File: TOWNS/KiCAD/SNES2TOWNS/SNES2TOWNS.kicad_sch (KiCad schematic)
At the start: 7 parts, among them J1 DE9_Receptacle, J2 Conn_01x06_Pin, J3 Conn_01x06_Pin, J4 Conn_01x06_Pin, J5 Conn_01x06_Pin, U1 74LS157, U2 74LS157

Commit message: Added bypass capacitor.
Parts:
- added C1, C2: 0.1uF, symbol Device:C
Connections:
- net +5V: now also C1.1, C2.1
- net GND: now also C1.2, C2.2
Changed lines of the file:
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@@
   (junction (at 153.67 91.44) (diameter 0) (color 0 0 0 0)
   )
+  (junction (at 242.57 95.25) (diameter 0) (color 0 0 0 0)
+  )
   (junction (at 226.06 95.25) (diameter 0) (color 0 0 0 0)
   )
@@
   )
   (junction (at 162.56 124.46) (diameter 0) (color 0 0 0 0)
+  )
+  (junction (at 223.52 81.28) (diameter 0) (color 0 0 0 0)
+  )
+  (junction (at 229.87 95.25) (diameter 0) (color 0 0 0 0)
+  )
+  (junction (at 229.87 109.22) (diameter 0) (color 0 0 0 0)
   )
   (junction (at 63.5 59.69) (diameter 0) (color 0 0 0 0)
@@
     (stroke (width 0) (type default))
   )
+  (wire (pts (xy 229.87 95.25) (xy 242.57 95.25))
+    (stroke (width 0) (type default))
+  )
   (wire (pts (xy 201.93 69.85) (xy 218.44 69.85))
     (stroke (width 0) (type default))
@@
     (stroke (width 0) (type default))
   )
+  (wire (pts (xy 242.57 95.25) (xy 242.57 101.6))
+    (stroke (width 0) (type default))
+  )
   (wire (pts (xy 162.56 87.63) (xy 162.56 121.92))
     (stroke (width 0) (type default))
@@
     (stroke (width 0) (type default))
   )
+  (wire (pts (xy 223.52 109.22) (xy 229.87 109.22))
+    (stroke (width 0) (type default))
+  )
   (wire (pts (xy 142.24 109.22) (xy 176.53 109.22))
     (stroke (width 0) (type default))
@@
     (stroke (width 0) (type default))
   )
-  (wire (pts (xy 226.06 95.25) (xy 271.78 95.25))
+  (wire (pts (xy 226.06 95.25) (xy 229.87 95.25))
     (stroke (width 0) (type default))
   )
@@
     (stroke (width 0) (type default))
   )
+  (wire (pts (xy 229.87 109.22) (xy 242.57 109.22))
+    (stroke (width 0) (type default))
+  )
   (wire (pts (xy 201.93 62.23) (xy 220.98 62.23))
     (stroke (width 0) (type default))
@@
     (stroke (width 0) (type default))
   )
+  (wire (pts (xy 223.52 81.28) (xy 241.3 81.28))
+    (stroke (width 0) (type default))
+  )
   (wire (pts (xy 212.09 106.68) (xy 212.09 73.66))
     (stroke (width 0) (type default))
   )
-  (wire (pts (xy 204.47 81.28) (xy 241.3 81.28))
+  (wire (pts (xy 204.47 81.28) (xy 223.52 81.28))
     (stroke (width 0) (type default))
   )
@@
   )
   (wire (pts (xy 204.47 81.28) (xy 204.47 87.63))
+    (stroke (width 0) (type default))
+  )
+  (wire (pts (xy 229.87 95.25) (xy 229.87 101.6))
+    (stroke (width 0) (type default))
+  )
+  (wire (pts (xy 223.52 81.28) (xy 223.52 109.22))
+    (stroke (width 0) (type default))
+  )
+  (wire (pts (xy 242.57 95.25) (xy 271.78 95.25))
     (stroke (width 0) (type default))
   )
@@
     )
   )
+  (symbol (lib_id "Device:C") (at 229.87 105.41 0) (unit 1)
+    (in_bom yes) (on_board yes) (dnp no) (fields_autoplaced)
+    (property "Reference" "C1" (at 233.68 104.14 0)
+      (effects (font (size 1.27 1.27)) (justify left))
+    )
+    (property "Value" "0.1uF" (at 233.68 106.68 0)
+      (effects (font (size 1.27 1.27)) (justify left))
+    )
+    (property "Footprint" "" (at 230.8352 109.22 0)
+      (effects (font (size 1.27 1.27)) hide)
+    )
+    (property "Datasheet" "~" (at 229.87 105.41 0)
+      (effects (font (size 1.27 1.27)) hide)
+    )
+    (pin "1")
+    (pin "2")
+    (instances
+      (project "SNES2TOWNS"
+        (path "/d12ccb08-8752-4d3d-ad3b-4f570691df19"
+          (reference "C1") (unit 1)
+        )
+      )
+    )
+  )
   (symbol (lib_id "Connector:DE9_Receptacle") (at 248.92 73.66 0) (unit 1)
     (in_bom yes) (on_board yes) (dnp no) (fields_autoplaced)
@@
         )
       )
+    )
+  )
+  (symbol (lib_id "Device:C") (at 242.57 105.41 0) (unit 1)
+    (in_bom yes) (on_board yes) (dnp no) (fields_autoplaced)
+    (property "Reference" "C2" (at 246.38 104.14 0)
+      (effects (font (size 1.27 1.27)) (justify left))
+    )
+    (property "Value" "0.1uF" (at 246.38 106.68 0)
+      (effects (font (size 1.27 1.27)) (justify left))
+    )
+    (property "Footprint" "" (at 243.5352 109.22 0)
+      (effects (font (size 1.27 1.27)) hide)
+    )
+    (property "Datasheet" "~" (at 242.57 105.41 0)
+      (effects (font (size 1.27 1.27)) hide)
+    )
+    (pin "1")
+    (pin "2")
+    (instances
+      (project "SNES2TOWNS"
+        (path "/d12ccb08-8752-4d3d-ad3b-4f570691df19"
+          (reference "C2") (unit 1)
+        )
+      )

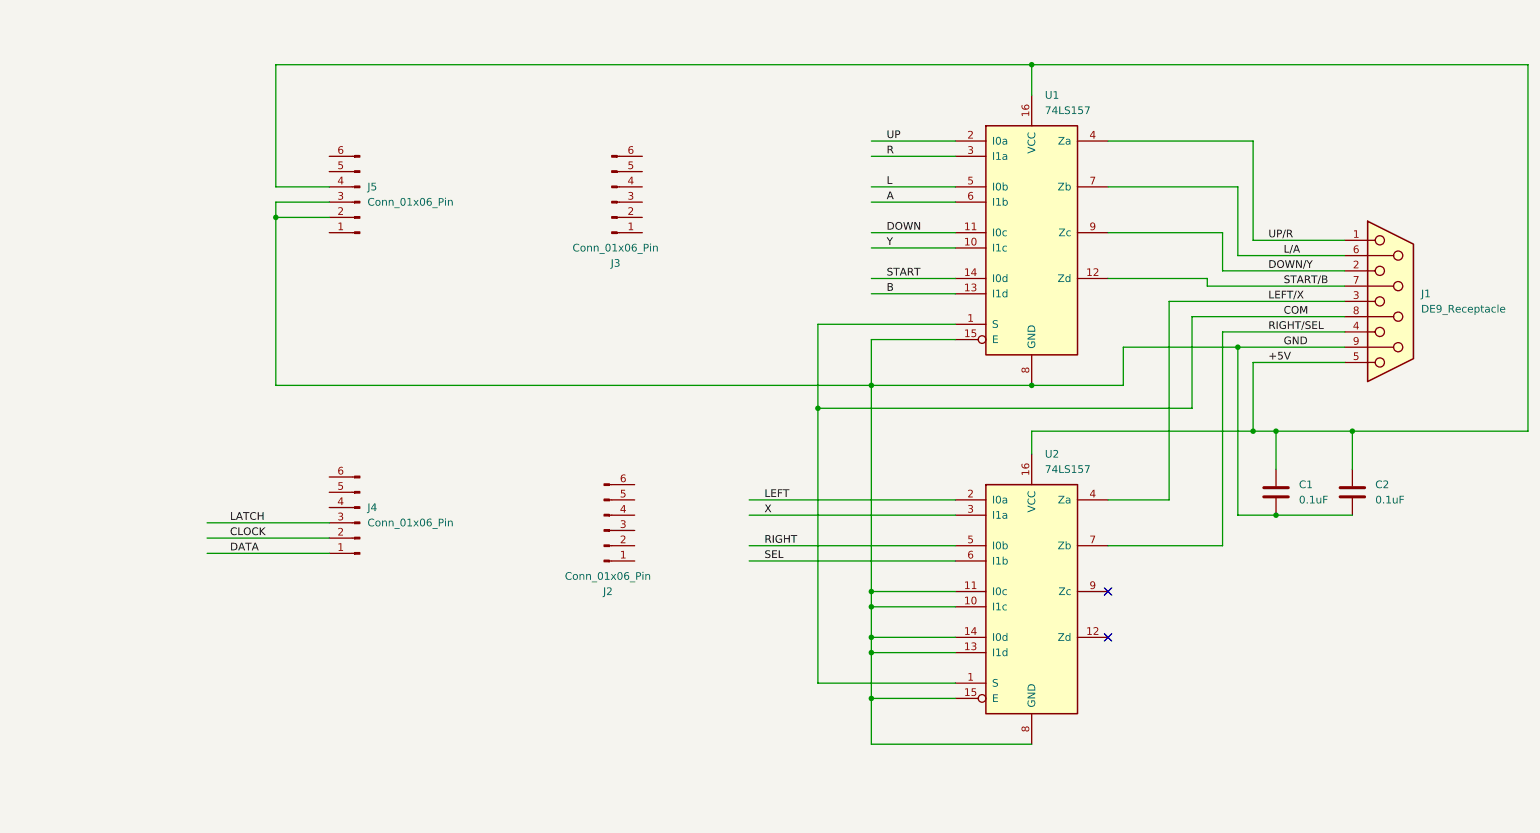
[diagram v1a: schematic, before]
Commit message: SNES to TOWNS Controller Adapter
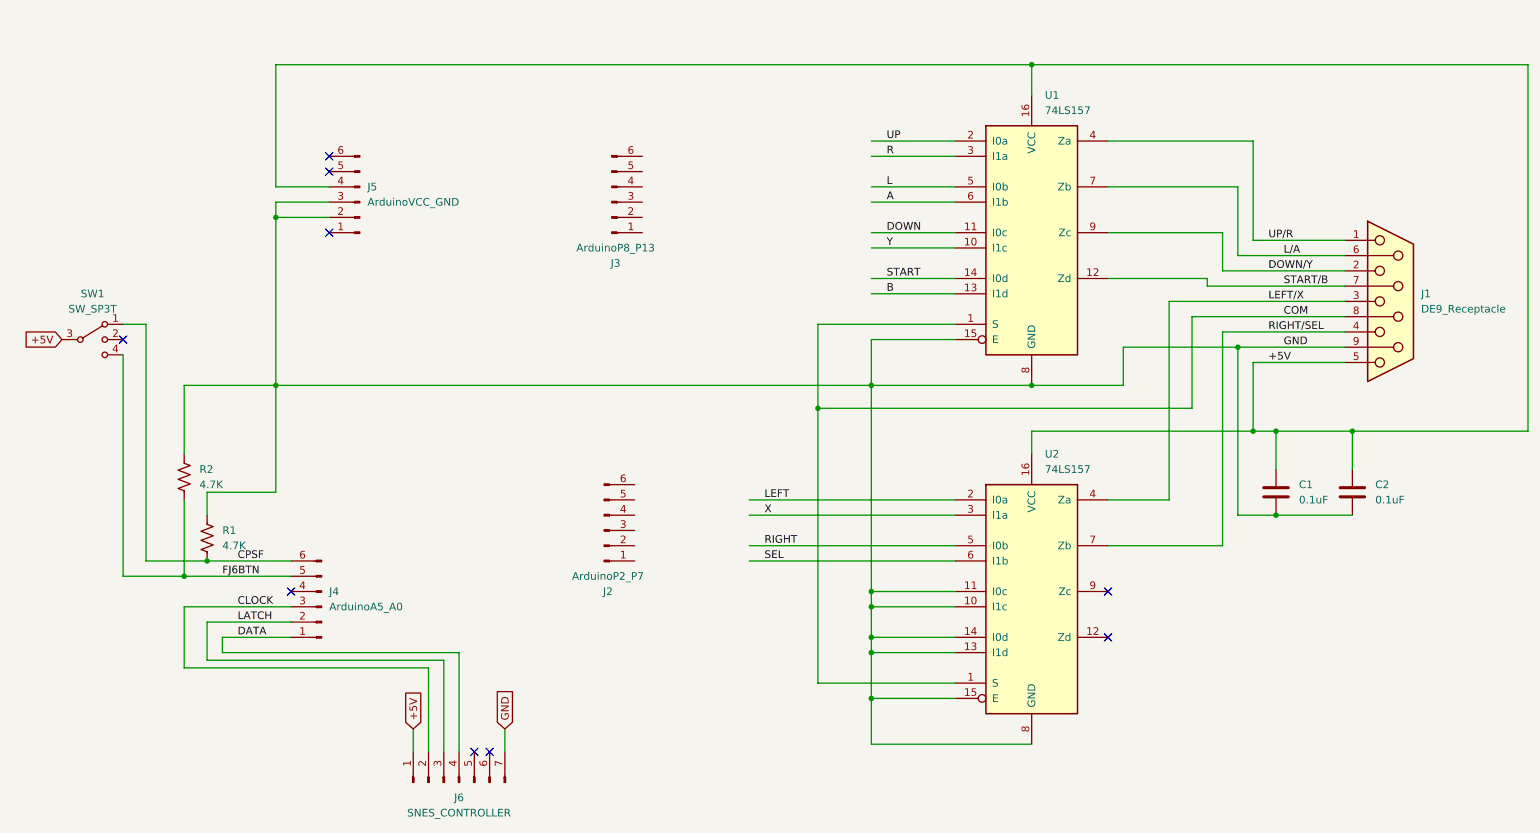
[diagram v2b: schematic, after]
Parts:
- added J6: SNES_CONTROLLER, symbol Connector:Conn_01x07_Pin
- added R1, R2: 4.7K, symbol Device:R_US
- added SW1: SW_SP3T, symbol Switch:SW_SP3T
- J2: value Conn_01x06_Pin -> ArduinoP2_P7
- J3: value Conn_01x06_Pin -> ArduinoP8_P13
- J4: value Conn_01x06_Pin -> ArduinoA5_A0
- J5: value Conn_01x06_Pin -> ArduinoVCC_GND
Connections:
- net +5V: now also J6.1 (Pin_1), SW1.3
- net CLOCK: now also J4.3 (Pin_3), J6.2 (Pin_2); no longer J4.2 (Pin_2)
- net DATA: now also J6.4 (Pin_4)
- net GND: now also J6.7 (Pin_7), R1.1, R2.1
- net LATCH: now also J4.2 (Pin_2), J6.3 (Pin_3); no longer J4.3 (Pin_3)
- net FJ6BTN: now reaches J4.5 (Pin_5)
- net FJ6BTN: now also R2.2, SW1.4
- net CPSF: now reaches J4.6 (Pin_6)
- net CPSF: now also R1.2, SW1.1
- no-connect marks 2 -> 9
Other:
- moved on the sheet: J4

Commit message: Rough PCB placements
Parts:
- removed SW1: SW_SP3T, symbol Switch:SW_SP3T
- added J7: Conn_02x03_Odd_Even, Connector_PinHeader_2.54mm:PinHeader_2x03_P2.54mm_Vertical, symbol Connector_Generic:Conn_02x03_Odd_Even
- C1, C2: footprint (none) -> Capacitor_THT:C_Disc_D5.0mm_W2.5mm_P5.00mm
- J1: footprint (none) -> Connector_Dsub:DSUB-9_Female_Vertical_P2.77x2.84mm
- J2, J3, J4, J5: footprint (none) -> Connector_PinHeader_2.54mm:PinHeader_1x06_P2.54mm_Vertical
- J6: footprint (none) -> Connector_PinHeader_2.54mm:PinHeader_1x07_P2.54mm_Vertical
- R1, R2: footprint (none) -> Resistor_THT:R_Axial_DIN0207_L6.3mm_D2.5mm_P10.16mm_Horizontal
- U1, U2: footprint (none) -> Package_DIP:DIP-16_W7.62mm_Socket
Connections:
- net +5V: now also J7.3 (Pin_3), J7.4 (Pin_4)
- net CPSF: now also J7.1 (Pin_1), J7.2 (Pin_2)
- net FJ6BTN: now also J7.5 (Pin_5), J7.6 (Pin_6)
- no-connect marks 9 -> 8
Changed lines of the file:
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@@
   (junction (at 162.56 121.92) (diameter 0) (color 0 0 0 0)
   )
+  (junction (at 38.1 87.63) (diameter 0) (color 0 0 0 0)
+  )
   (junction (at 162.56 132.08) (diameter 0) (color 0 0 0 0)
   )
+  (junction (at 44.45 80.01) (diameter 0) (color 0 0 0 0)
+  )
   (junction (at 52.07 116.84) (diameter 0) (color 0 0 0 0)
   )
@@
   )
   (junction (at 48.26 119.38) (diameter 0) (color 0 0 0 0)
+  )
+  (junction (at 38.1 77.47) (diameter 0) (color 0 0 0 0)
   )
   (junction (at 63.5 87.63) (diameter 0) (color 0 0 0 0)
@@
   (no_connect (at 66.04 121.92))
   (no_connect (at 99.06 148.59))
-  (no_connect (at 38.1 80.01))
   (no_connect (at 96.52 148.59))
   (no_connect (at 72.39 52.07))
@@
     (stroke (width 0) (type default))
   )
+  (wire (pts (xy 38.1 71.12) (xy 25.4 71.12))
+    (stroke (width 0) (type default))
+  )
   (wire (pts (xy 271.78 95.25) (xy 271.78 34.29))
     (stroke (width 0) (type default))
@@
     (stroke (width 0) (type default))
   )
+  (wire (pts (xy 44.45 80.01) (xy 45.72 80.01))
+    (stroke (width 0) (type default))
+  )
   (wire (pts (xy 201.93 54.61) (xy 223.52 54.61))
     (stroke (width 0) (type default))
   )
+  (wire (pts (xy 38.1 77.47) (xy 38.1 71.12))
+    (stroke (width 0) (type default))
+  )
   (wire (pts (xy 162.56 46.99) (xy 176.53 46.99))
     (stroke (width 0) (type default))
@@
     (stroke (width 0) (type default))
   )
+  (wire (pts (xy 25.4 71.12) (xy 25.4 77.47))
+    (stroke (width 0) (type default))
+  )
   (wire (pts (xy 218.44 69.85) (xy 218.44 71.12))
     (stroke (width 0) (type default))
@@
     (stroke (width 0) (type default))
   )
+  (wire (pts (xy 44.45 67.31) (xy 21.59 67.31))
+    (stroke (width 0) (type default))
+  )
   (wire (pts (xy 220.98 114.3) (xy 220.98 78.74))
     (stroke (width 0) (type default))
@@
     (stroke (width 0) (type default))
   )
+  (wire (pts (xy 21.59 80.01) (xy 25.4 80.01))
+    (stroke (width 0) (type default))
+  )
   (wire (pts (xy 226.06 46.99) (xy 226.06 63.5))
     (stroke (width 0) (type default))
@@
     (stroke (width 0) (type default))
   )
+  (wire (pts (xy 21.59 67.31) (xy 21.59 80.01))
+    (stroke (width 0) (type default))
+  )
   (wire (pts (xy 189.23 34.29) (xy 189.23 39.37))
     (stroke (width 0) (type default))
@@
     (stroke (width 0) (type default))
   )
+  (wire (pts (xy 25.4 82.55) (xy 25.4 87.63))
+    (stroke (width 0) (type default))
+  )
   (wire (pts (xy 38.1 77.47) (xy 41.91 77.47))
     (stroke (width 0) (type default))
@@
     (stroke (width 0) (type default))
   )
+  (wire (pts (xy 38.1 87.63) (xy 38.1 119.38))
+    (stroke (width 0) (type default))
+  )
   (wire (pts (xy 223.52 81.28) (xy 241.3 81.28))
     (stroke (width 0) (type default))
@@
     (stroke (width 0) (type default))
   )
+  (wire (pts (xy 38.1 80.01) (xy 44.45 80.01))
+    (stroke (width 0) (type default))
+  )
   (wire (pts (xy 54.61 132.08) (xy 93.98 132.08))
     (stroke (width 0) (type default))
@@
     (stroke (width 0) (type default))
   )
-  (wire (pts (xy 38.1 82.55) (xy 38.1 119.38))
+  (wire (pts (xy 38.1 82.55) (xy 38.1 87.63))
     (stroke (width 0) (type default))
   )
@@
     (stroke (width 0) (type default))
   )
+  (wire (pts (xy 25.4 87.63) (xy 38.1 87.63))
+    (stroke (width 0) (type default))
+  )
   (wire (pts (xy 204.47 81.28) (xy 204.47 87.63))
     (stroke (width 0) (type default))
@@
     (stroke (width 0) (type default))
   )
+  (wire (pts (xy 44.45 80.01) (xy 44.45 67.31))
+    (stroke (width 0) (type default))
+  )
   (wire (pts (xy 223.52 66.04) (xy 241.3 66.04))
     (stroke (width 0) (type default))
@@
     (effects (font (size 1.27 1.27)) (justify left bottom))
   )
-  (global_label "+5V" (shape input) (at 27.94 80.01 180) (fields_autoplaced)
-    (effects (font (size 1.27 1.27)) (justify right))
-    (property "Intersheetrefs" "${INTERSHEET_REFS}" (at 21.0843 80.01 0)
-      (effects (font (size 1.27 1.27)) (justify right) hide)
+  (global_label "+5V" (shape input) (at 45.72 80.01 0) (fields_autoplaced)
+    (effects (font (size 1.27 1.27)) (justify left))
+    (property "Intersheetrefs" "${INTERSHEET_REFS}" (at 52.5757 80.01 0)
+      (effects (font (size 1.27 1.27)) (justify left) hide)
     )
   )
@@
       (effects (font (size 1.27 1.27)))
     )
-    (property "Footprint" "" (at 93.98 153.67 0)
+    (property "Footprint" "Connector_PinHeader_2.54mm:PinHeader_1x07_P2.54mm_Vertical" (at 93.98 153.67 0)
       (effects (font (size 1.27 1.27)) hide)
     )
@@
       (effects (font (size 1.27 1.27)) (justify left))
     )
-    (property "Footprint" "" (at 189.23 121.92 0)
+    (property "Footprint" "Package_DIP:DIP-16_W7.62mm_Socket" (at 189.23 121.92 0)
       (effects (font (size 1.27 1.27)) hide)
     )
@@
       (effects (font (size 1.27 1.27)))
     )
-    (property "Footprint" "" (at 118.11 111.76 0)
+    (property "Footprint" "Connector_PinHeader_2.54mm:PinHeader_1x06_P2.54mm_Vertical" (at 118.11 111.76 0)
       (effects (font (size 1.27 1.27)) hide)
     )
@@
       (effects (font (size 1.27 1.27)) (justify left))
     )
-    (property "Footprint" "" (at 49.276 103.124 90)
+    (property "Footprint" "Resistor_THT:R_Axial_DIN0207_L6.3mm_D2.5mm_P10.16mm_Horizontal" (at 49.276 103.124 90)
       (effects (font (size 1.27 1.27)) hide)
     )
@@
       (effects (font (size 1.27 1.27)) (justify left))
     )
-    (property "Footprint" "" (at 53.086 113.284 90)
+    (property "Footprint" "Resistor_THT:R_Axial_DIN0207_L6.3mm_D2.5mm_P10.16mm_Horizontal" (at 53.086 113.284 90)
       (effects (font (size 1.27 1.27)) hide)
     )
@@
       (effects (font (size 1.27 1.27)) (justify right))
     )
-    (property "Footprint" "" (at 71.12 124.46 0)
+    (property "Footprint" "Connector_PinHeader_2.54mm:PinHeader_1x06_P2.54mm_Vertical" (at 71.12 124.46 0)
       (effects (font (size 1.27 1.27)) hide)
     )
@@
       (effects (font (size 1.27 1.27)) (justify right))
     )
-    (property "Footprint" "" (at 77.47 57.15 0)
+    (property "Footprint" "Connector_PinHeader_2.54mm:PinHeader_1x06_P2.54mm_Vertical" (at 77.47 57.15 0)
       (effects (font (size 1.27 1.27)) hide)
     )
@@
     )
   )
+  (symbol (lib_id "Connector_Generic:Conn_02x03_Odd_Even") (at 30.48 80.01 0) (unit 1)
+    (in_bom yes) (on_board yes) (dnp no) (fields_autoplaced)
+    (property "Reference" "J7" (at 31.75 71.12 0)
+      (effects (font (size 1.27 1.27)))
+    )
+    (property "Value" "Conn_02x03_Odd_Even" (at 31.75 73.66 0)
+      (effects (font (size 1.27 1.27)))
+    )
+    (property "Footprint" "Connector_PinHeader_2.54mm:PinHeader_2x03_P2.54mm_Vertical" (at 30.48 80.01 0)
+      (effects (font (size 1.27 1.27)) hide)
+    )
+    (property "Datasheet" "~" (at 30.48 80.01 0)
+      (effects (font (size 1.27 1.27)) hide)
+    )
+    (pin "1")
+    (pin "2")
+    (pin "3")
+    (pin "4")
+    (pin "5")
+    (pin "6")
+    (instances
+      (project "SNES2TOWNS"
+        (path "/d12ccb08-8752-4d3d-ad3b-4f570691df19"
+          (reference "J7") (unit 1)
+        )
+      )
+    )
+  )
   (symbol (lib_id "Device:C") (at 229.87 105.41 0) (unit 1)
     (in_bom yes) (on_board yes) (dnp no) (fields_autoplaced)
@@
       (effects (font (size 1.27 1.27)) (justify left))
     )
-    (property "Footprint" "" (at 230.8352 109.22 0)
+    (property "Footprint" "Capacitor_THT:C_Disc_D5.0mm_W2.5mm_P5.00mm" (at 230.8352 109.22 0)
       (effects (font (size 1.27 1.27)) hide)
     )
@@
       (effects (font (size 1.27 1.27)) (justify left))
     )
-    (property "Footprint" "" (at 248.92 73.66 0)
+    (property "Footprint" "Connector_Dsub:DSUB-9_Female_Vertical_P2.77x2.84mm" (at 248.92 73.66 0)
       (effects (font (size 1.27 1.27)) hide)
     )
@@
       (effects (font (size 1.27 1.27)) (justify left))
     )
-    (property "Footprint" "" (at 243.5352 109.22 0)
+    (property "Footprint" "Capacitor_THT:C_Disc_D5.0mm_W2.5mm_P5.00mm" (at 243.5352 109.22 0)
       (effects (font (size 1.27 1.27)) hide)
     )
@@
       (effects (font (size 1.27 1.27)) (justify left))
     )
-    (property "Footprint" "" (at 189.23 62.23 0)
+    (property "Footprint" "Package_DIP:DIP-16_W7.62mm_Socket" (at 189.23 62.23 0)
       (effects (font (size 1.27 1.27)) hide)
     )
@@
     )
   )
-  (symbol (lib_id "Switch:SW_SP3T") (at 33.02 80.01 0) (unit 1)
-    (in_bom yes) (on_board yes) (dnp no) (fields_autoplaced)
-    (property "Reference" "SW1" (at 33.02 72.39 0)
-      (effects (font (size 1.27 1.27)))
-    )
-    (property "Value" "SW_SP3T" (at 33.02 74.93 0)
-      (effects (font (size 1.27 1.27)))
-    )
-    (property "Footprint" "" (at 17.145 75.565 0)
-      (effects (font (size 1.27 1.27)) hide)
-    )
-    (property "Datasheet" "~" (at 17.145 75.565 0)
-      (effects (font (size 1.27 1.27)) hide)
-    )
-    (pin "1")
-    (pin "2")
-    (pin "3")
-    (pin "4")
-    (instances
-      (project "SNES2TOWNS"
-        (path "/d12ccb08-8752-4d3d-ad3b-4f570691df19"
-          (reference "SW1") (unit 1)
-        )
-      )
-    )
-  )
   (symbol (lib_id "Connector:Conn_01x06_Pin") (at 119.38 57.15 0) (mirror x) (unit 1)
     (in_bom yes) (on_board yes) (dnp no)
@@
       (effects (font (size 1.27 1.27)))
     )
-    (property "Footprint" "" (at 119.38 57.15 0)
-      (effects (font (size 1.27 1.27)) hide)
-    )
+    (property "Footprint" "Connector_PinHeader_2.54mm:PinHeader_1x06_P2.54mm_Vertical" (at 119.38 57.15 0)
+      (effects (font (size 1.27 1.27)) hide)
+    )
